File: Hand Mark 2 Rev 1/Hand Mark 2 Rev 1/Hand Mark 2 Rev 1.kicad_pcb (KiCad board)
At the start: 2 copper layers, 34 parts, among them J1 Conn_ARM_JTAG_SWD_10, M1 Index_Servo, M2 Middle_Servo, M3 Ring_Servo, M4 Pinky_Servo, M5 Thumb_Servo, SW1 Power_Switch

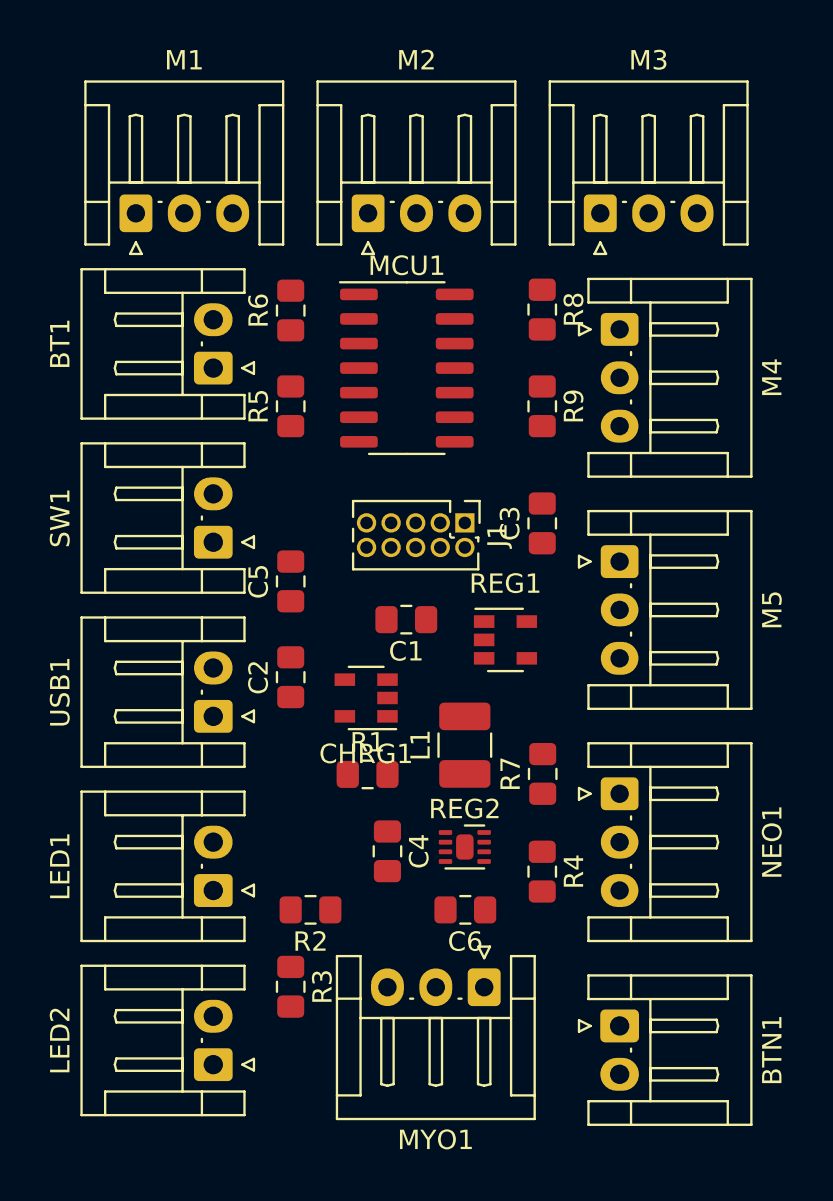
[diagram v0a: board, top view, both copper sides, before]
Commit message: moved parts to put logic on bottom of board
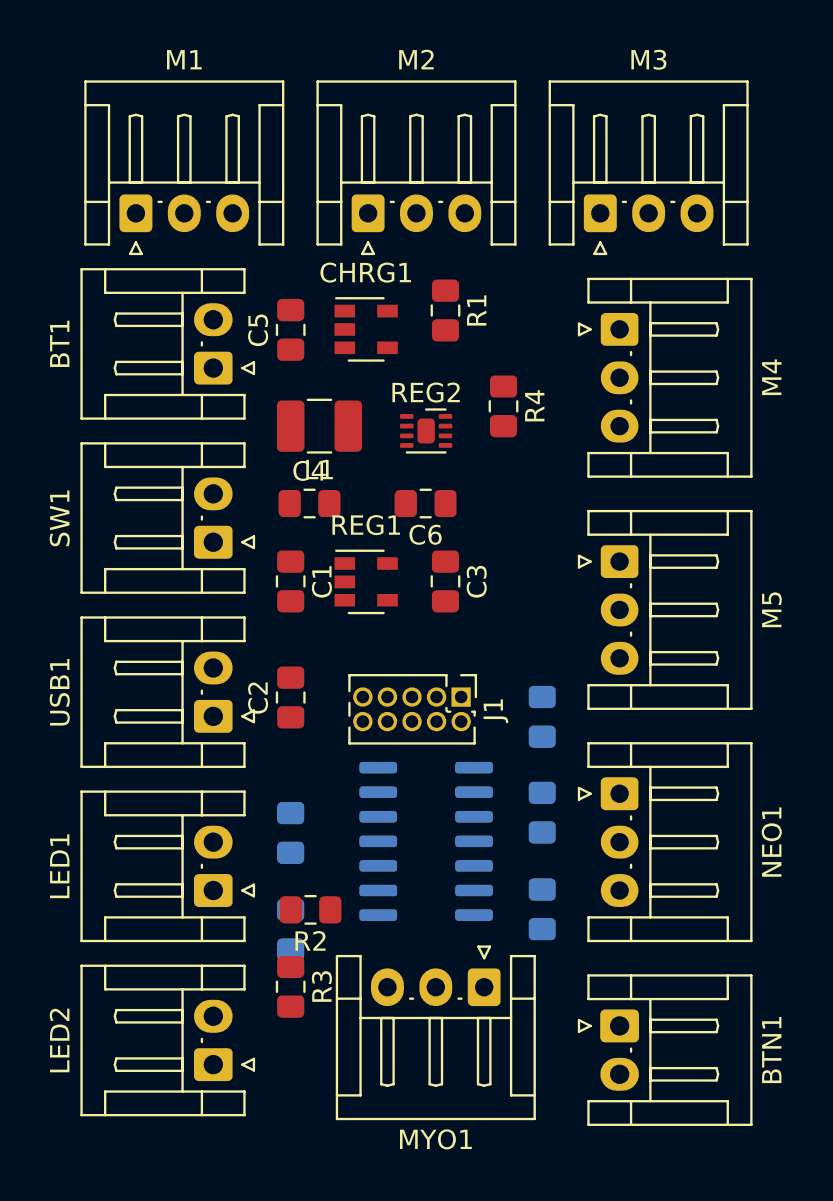
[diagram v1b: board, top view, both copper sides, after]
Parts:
- MCU1, R5, R6, R7, R8, R9: moved to B.Cu
- moved R6 32.0 mm to (126.0, 63.0), turned to 270 degrees
- moved R8 31.0 mm to (139.0, 62.0), turned to 90 degrees
- moved MCU1 24.5 mm to (133.0, 58.5)
- moved R1 24.3 mm to (134.0, 31.0), turned to 270 degrees
- moved R4 24.1 mm to (137.0, 36.0)
- moved R5 22.0 mm to (126.0, 58.0), turned to 270 degrees
- moved REG2 21.6 mm to (133.0, 37.2)
- moved C6 21.1 mm to (133.0, 41.0)
- moved R9 21.0 mm to (139.0, 57.0), turned to 90 degrees
- moved CHRG1 19.0 mm to (129.9, 32.0), turned to 0 degrees
- moved C4 18.4 mm to (127.0, 41.0), turned to 0 degrees
- moved L1 18.1 mm to (127.5, 37.0), turned to 180 degrees
- moved C5 13.0 mm to (126.0, 32.0)
- moved J1 9.00 mm to (134.8, 51.0)
- moved REG1 7.80 mm to (129.9, 45.0)
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
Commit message: finsihed first test routing(need thicker traces for power)
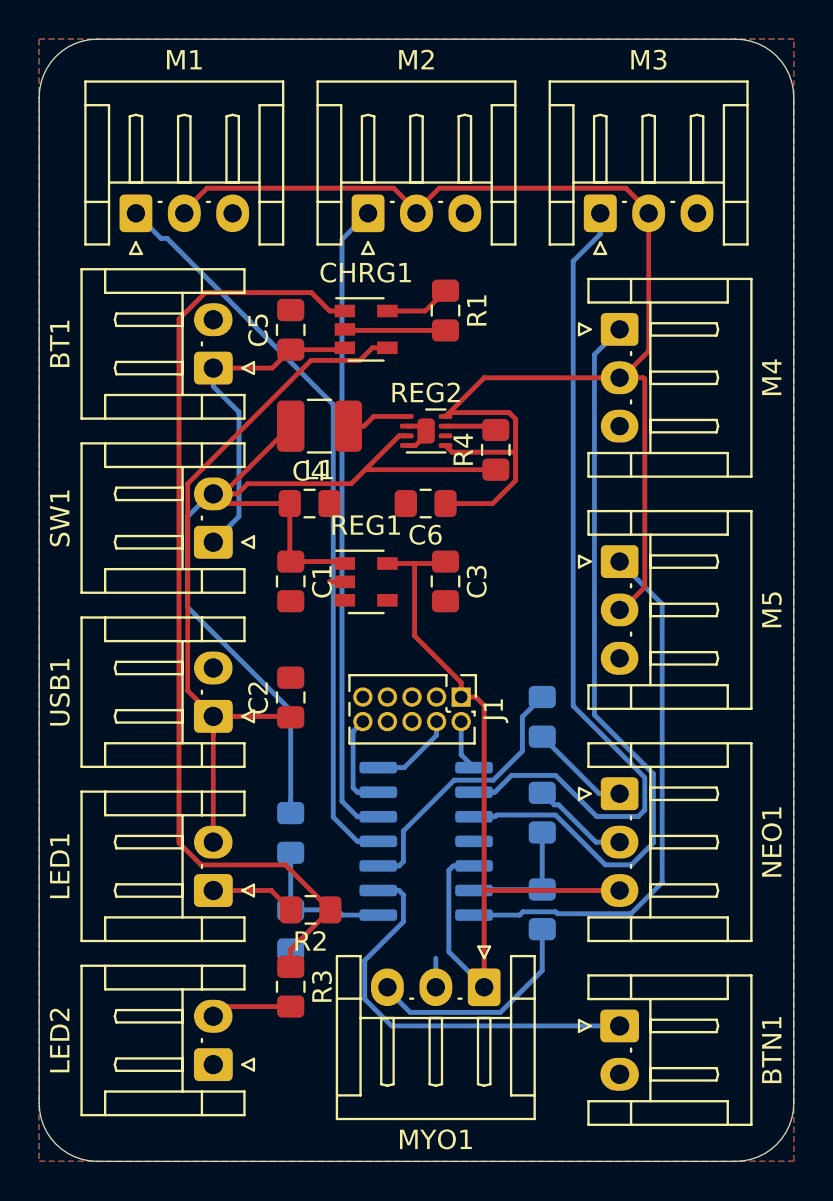
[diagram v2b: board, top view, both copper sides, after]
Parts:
- moved R4 2.29 mm to (136.6, 38.2), turned to 90 degrees
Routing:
- net +5V: track 0.00 -> 74.1 mm
- net +BATT: track 0.00 -> 52.8 mm
- net Net-(CHRG1-Pad1): track 0.00 -> 49.7 mm
- net RING: track 0.00 -> 43.2 mm
- net +3V3: track 0.00 -> 42.1 mm
- net PINKY: track 0.00 -> 39.2 mm
- net INDEX: track 0.00 -> 38.5 mm
- net Net-(C2-Pad1): track 0.00 -> 36.3 mm
- net MIDDLE: track 0.00 -> 33.2 mm
- net THUMB: track 0.00 -> 28.0 mm
- net BTN: track 0.00 -> 21.4 mm
- net Net-(BT1-Pad1): track 0.00 -> 17.3 mm
- net NEO: track 0.00 -> 14.1 mm
- net MYOSIG: track 0.00 -> 11.6 mm
- net GND: track 0.00 -> 9.90 mm
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- added copper zone on B.Cu, net GND
- added copper zone on F.Cu, net GND
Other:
- board outline added: 39 x 58 mm

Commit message: added bigger traces to servo power but should be double checked
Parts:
- added R10: 1000ohm, Resistor_SMD:R_0805_2012Metric_Pad1.15x1.40mm_HandSolder, F.Cu at (134.7, 55.7)
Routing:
- net Net-(J1-Pad4): track 4.42 -> 7.90 mm
- net +BATT: track 52.8 -> 49.4 mm, vias 0 -> 2
- net GND: track 9.90 -> 12.8 mm
- net +3V3: track 42.1 -> 44.5 mm
- net +5V: track 74.1 -> 76.3 mm
- net Net-(BT1-Pad1): track 17.3 -> 19.1 mm
